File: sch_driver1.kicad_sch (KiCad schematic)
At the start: 17 parts, among them Q1 PSMN4R0-30YLDX, U1 ADA4099-2xR, U11 TS5A3159ADCK, U21 OPA333

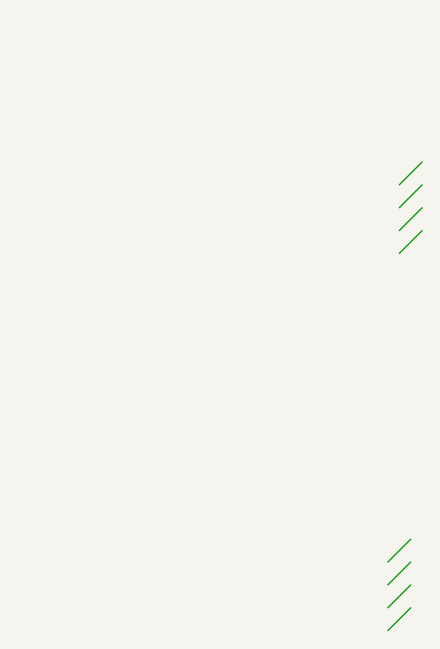
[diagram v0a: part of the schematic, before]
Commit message: Finished schematic refactor to six A-sheets. Updated PCB.
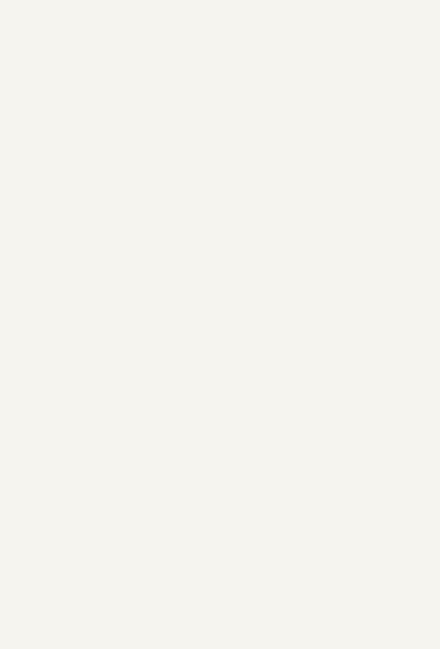
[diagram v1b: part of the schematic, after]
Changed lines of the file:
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@@
 	(title_block
 		(title "PBM Driver 4 V2")
-		(date "23-DEC-2025")
+		(date "24-DEC-2025")
 		(rev "A")
 		(comment 1 "Part Number: PCB104 Rev A")
@@
 		(color 0 0 0 0)
 	)
-	(bus_entry
-		(at 389.89 226.06)
-		(size -2.54 2.54)
-		(stroke
-			(width 0)
-			(type default)
-		)
-	)
-	(bus_entry
-		(at 389.89 223.52)
-		(size -2.54 2.54)
-		(stroke
-			(width 0)
-			(type default)
-		)
-	)
-	(bus_entry
-		(at 391.16 181.61)
-		(size -2.54 2.54)
-		(stroke
-			(width 0)
-			(type default)
-		)
-	)
-	(bus_entry
-		(at 391.16 179.07)
-		(size -2.54 2.54)
-		(stroke
-			(width 0)
-			(type default)
-		)
-	)
-	(bus_entry
-		(at 389.89 220.98)
-		(size -2.54 2.54)
-		(stroke
-			(width 0)
-			(type default)
-		)
-	)
-	(bus_entry
-		(at 391.16 184.15)
-		(size -2.54 2.54)
-		(stroke
-			(width 0)
-			(type default)
-		)
-	)
-	(bus_entry
-		(at 391.16 176.53)
-		(size -2.54 2.54)
-		(stroke
-			(width 0)
-			(type default)
-		)
-	)
-	(bus_entry
-		(at 389.89 218.44)
-		(size -2.54 2.54)
-		(stroke
-			(width 0)
-			(type default)
-		)
-	)
 	(wire

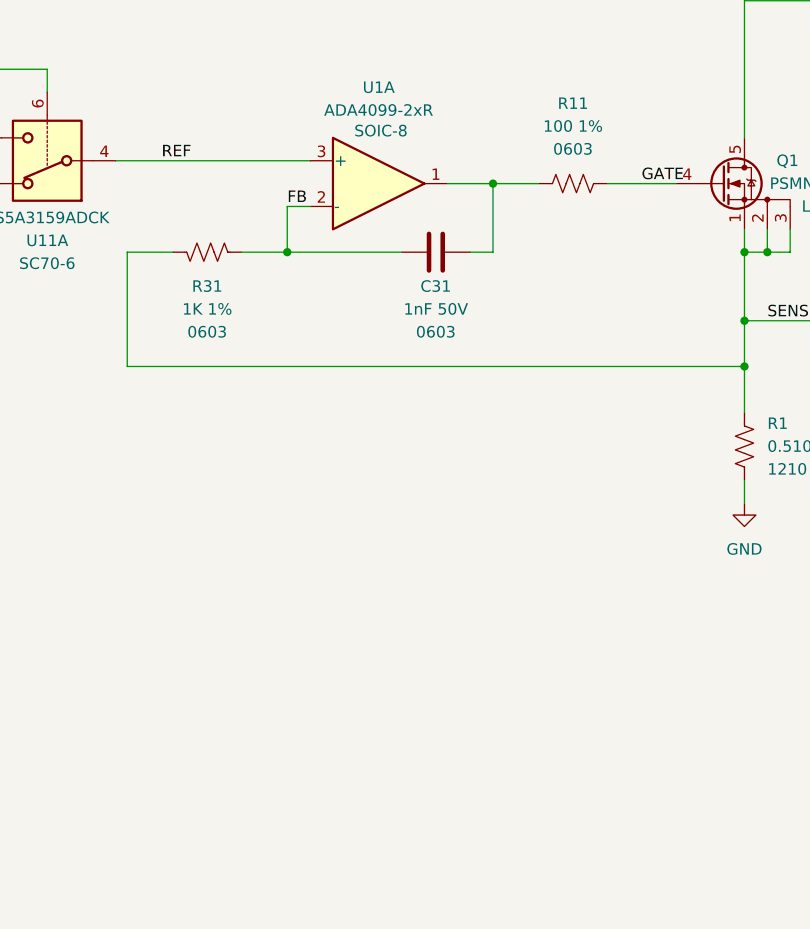
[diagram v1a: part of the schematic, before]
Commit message: Routing WIP. Prep to look at SOT-23 op amps for U1 and U2. Added convenience link to Git Bash.
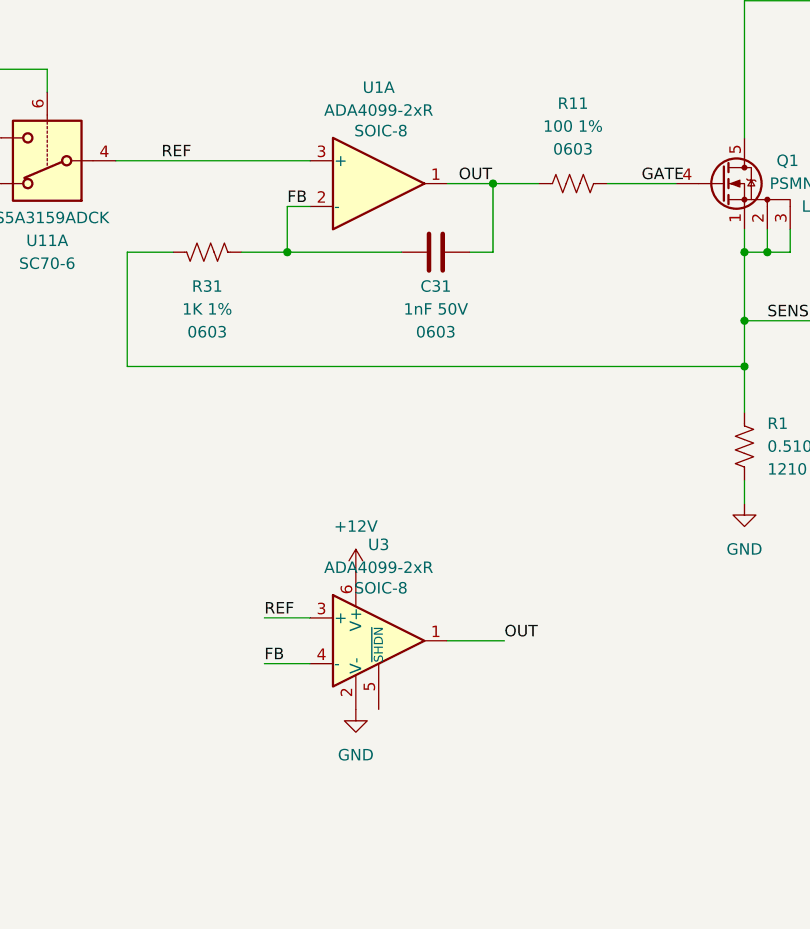
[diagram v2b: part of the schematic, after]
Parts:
- added U3: ADA4099-2xR, Package_TO_SOT_SMD:TSOT-23-6, symbol Amplifier_Operational:ADA4099-1xUJ
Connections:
- net +12V: now also U3.6 (V+)
- net FB: now also U3.4 (-)
- net GND: now also U3.2 (V-)
- net REF: now also U3.3 (+)
- net OUT: now reaches C31.2, R11.1, U1.1
- net OUT: now also U3.1

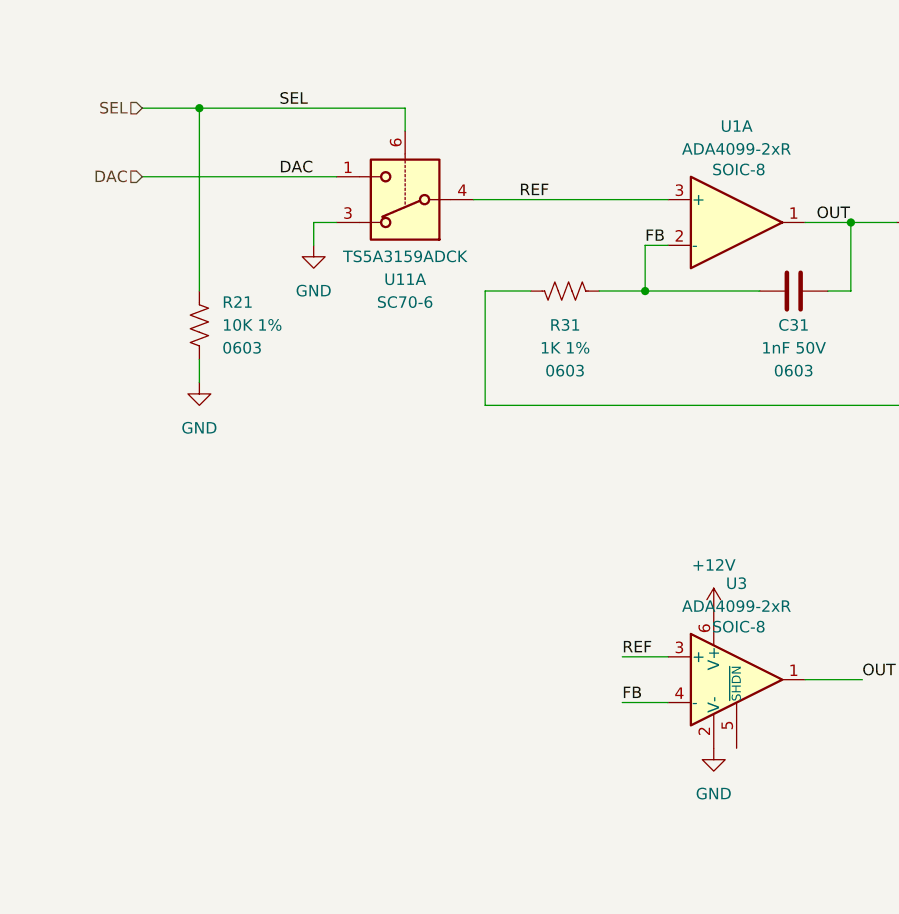
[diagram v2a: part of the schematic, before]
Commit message: Routing WIP with SOT-23 op amps
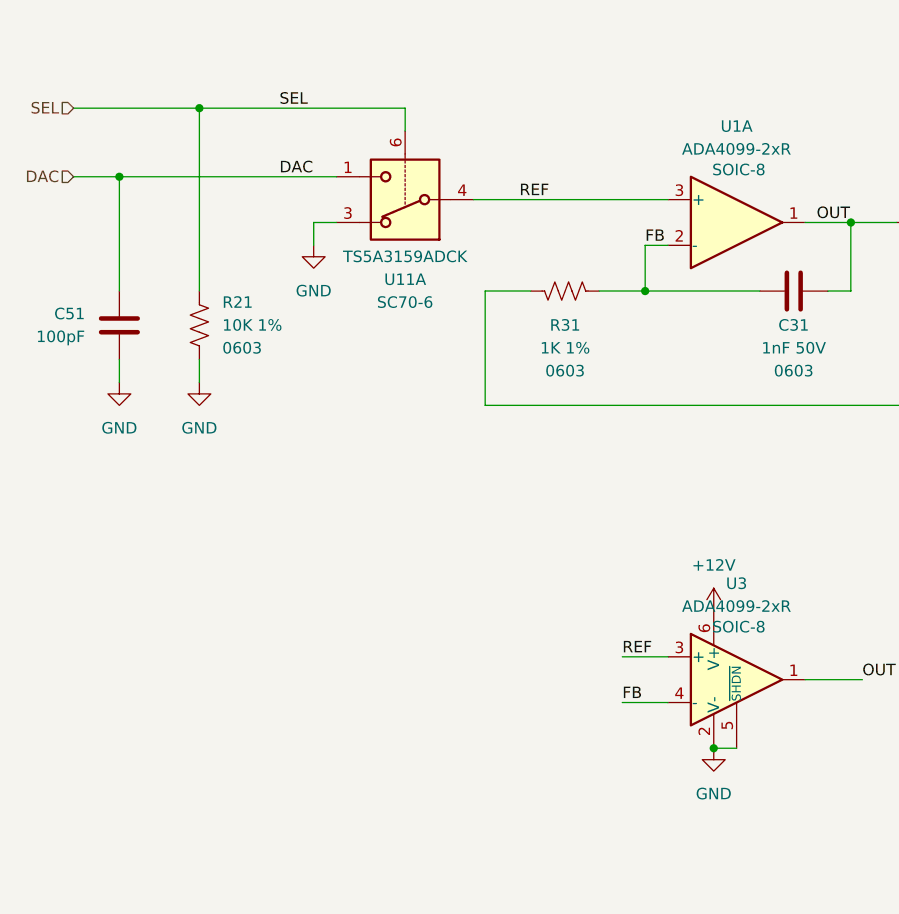
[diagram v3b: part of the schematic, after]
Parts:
- added C51: 100pF, $Local:C_0603_1608Metric, symbol $Local:C
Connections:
- net DAC: now also C51.1
- net GND: now also U3.5 (~{SHDN}), C51.2
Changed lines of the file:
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@@
+	)
+	(junction
+		(at 33.02 48.26)
+		(diameter 0)
+		(color 0 0 0 0)
 	)
 	(junction
@@
 	)
 	(junction
+		(at 99.06 111.76)
+		(diameter 0)
+		(color 0 0 0 0)
+	)
+	(junction
 		(at 95.25 147.32)
 		(diameter 0)
@@
 	(wire
 		(pts
+			(xy 99.06 111.76) (xy 101.6 111.76)
+		)
+		(stroke
+			(width 0)
+			(type default)
+		)
+	)
+	(wire
+		(pts
 			(xy 118.11 177.8) (xy 95.25 177.8)
 		)
@@
 	(wire
 		(pts
+			(xy 33.02 48.26) (xy 33.02 60.96)
+		)
+		(stroke
+			(width 0)
+			(type default)
+		)
+	)
+	(wire
+		(pts
 			(xy 203.2 88.9) (xy 205.74 88.9)
 		)
@@
 	(wire
 		(pts
-			(xy 35.56 40.64) (xy 41.91 40.64)
+			(xy 27.94 40.64) (xy 41.91 40.64)
 		)
 		(stroke
@@
 	(wire
 		(pts
-			(xy 35.56 48.26) (xy 57.15 48.26)
+			(xy 27.94 48.26) (xy 33.02 48.26)
 		)
 		(stroke
@@
 	(wire
 		(pts
+			(xy 33.02 48.26) (xy 57.15 48.26)
+		)
+		(stroke
+			(width 0)
+			(type default)
+		)
+	)
+	(wire
+		(pts
 			(xy 213.36 43.18) (xy 220.98 43.18)
 		)
@@
 		(pts
 			(xy 73.66 177.8) (xy 73.66 181.61)
+		)
+		(stroke
+			(width 0)
+			(type default)
+		)
+	)
+	(wire
+		(pts
+			(xy 33.02 68.58) (xy 33.02 71.12)
 		)
 		(stroke
@@
 	(hierarchical_label "DAC"
 		(shape input)
-		(at 35.56 48.26 180)
+		(at 27.94 48.26 180)
 		(effects
 			(font
@@
 	(hierarchical_label "SEL"
 		(shape input)
-		(at 35.56 40.64 180)
+		(at 27.94 40.64 180)
 		(effects
 			(font
@@
 	)
 	(symbol
+		(lib_id "$Local:GND")
+		(at 33.02 71.12 0)
+		(unit 1)
+		(exclude_from_sim no)
+		(in_bom yes)
+		(on_board yes)
+		(dnp no)
+		(fields_autoplaced yes)
+		(property "Reference" "#PWR021"
+			(at 33.02 77.47 0)
+			(effects
+				(font
+					(size 1.27 1.27)
+				)
+				(hide yes)
+			)
+		)
+		(property "Value" "GND"
+			(at 33.02 76.2 0)
+			(effects
+				(font
+					(size 1.27 1.27)
+				)
+			)
+		)
+		(property "Footprint" ""
+			(at 33.02 71.12 0)
+			(effects
+				(font
+					(size 1.27 1.27)
+				)
+				(hide yes)
+			)
+		)
+		(property "Datasheet" ""
+			(at 33.02 71.12 0)
+			(effects
+				(font
+					(size 1.27 1.27)
+				)
+				(hide yes)
+			)
+		)
+		(property "Description" "Power symbol creates a global label with name \"GND\" , ground"
+			(at 33.02 71.12 0)
+			(effects
+				(font
+					(size 1.27 1.27)
+				)
+				(hide yes)
+			)
+		)
+		(pin "1"
+		)
+		(instances
+			(project "pbm_driver4_v2"
+				(path "/04797749-7aaf-42f7-a5f4-0b9aeb0ad7be/69524e69-370d-45a1-972c-d2766add5424"
+					(reference "#PWR021")
+					(unit 1)
+				)
+			)
+		)
+	)
+	(symbol
 		(lib_id "$Local:C_0603_1NF_50V")
 		(at 184.15 73.66 0)
@@
 					(unit 1)
 				)
+			)
+		)
+	)
+	(symbol
+		(lib_id "$Local:C")
+		(at 33.02 64.77 0)
+		(unit 1)
+		(exclude_from_sim no)
+		(in_bom yes)
+		(on_board yes)
+		(dnp no)
+		(property "Reference" "C51"
+			(at 29.21 63.4999 0)
+			(effects
+				(font
+					(size 1.27 1.27)
+				)
+				(justify right)
+			)
+		)
+		(property "Value" "100pF"
+			(at 29.21 66.0399 0)
+			(effects
+				(font
+					(size 1.27 1.27)
+				)
+				(justify right)
+			)
+		)
+		(property "Footprint" "$Local:C_0603_1608Metric"
+			(at 33.9852 68.58 0)
+			(effects
+				(font
+					(size 1.27 1.27)
+				)
+				(hide yes)
+			)
+		)
+		(property "Datasheet" "~"
+			(at 33.02 64.77 0)
+			(effects
+				(font
+					(size 1.27 1.27)
+				)
+				(hide yes)
+			)
+		)
+		(property "Description" "Unpolarized capacitor"
+			(at 33.02 64.77 0)
+			(effects
+				(font
+					(size 1.27 1.27)
+				)
+				(hide yes)
+			)
+		)
+		(pin "2"
+		)
+		(pin "1"
+		)
+		(instances
+			(project ""
+				(path "/04797749-7aaf-42f7-a5f4-0b9aeb0ad7be/69524e69-370d-45a1-972c-d2766add5424"
+					(reference "C51")
+					(unit 1)
+				)

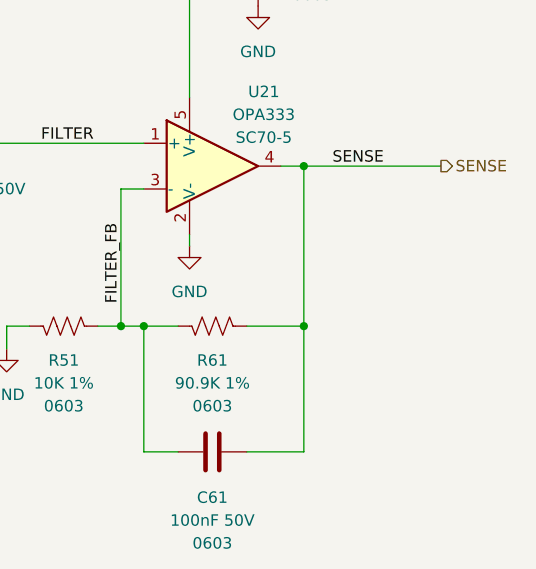
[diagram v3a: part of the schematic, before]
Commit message: Added pull-downs to output of Sense filter op amps
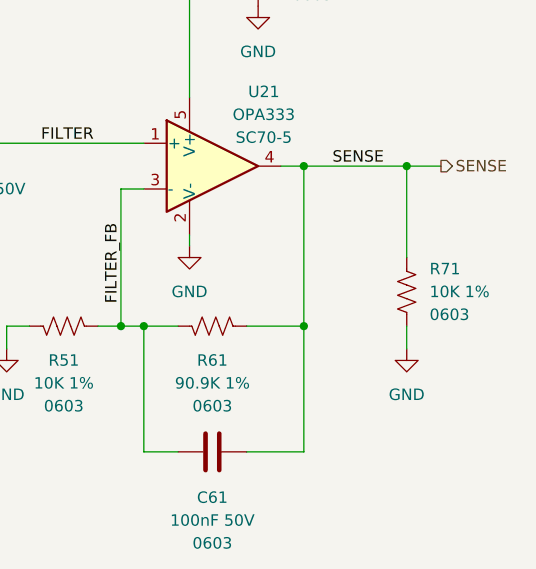
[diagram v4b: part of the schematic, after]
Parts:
- added R71: 10K 1%, $Local:R_0603_1608Metric, symbol $Local:R_0603_10K
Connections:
- net GND: now also R71.2
- net SENSE: now also R71.1
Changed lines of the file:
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@@
 	)
 	(junction
+		(at 237.49 71.12)
+		(diameter 0)
+		(color 0 0 0 0)
+	)
+	(junction
 		(at 95.25 147.32)
 		(diameter 0)
@@
 	(wire
 		(pts
+			(xy 237.49 71.12) (xy 237.49 81.28)
+		)
+		(stroke
+			(width 0)
+			(type default)
+		)
+	)
+	(wire
+		(pts
 			(xy 33.02 48.26) (xy 57.15 48.26)
 		)
@@
 	(wire
 		(pts
+			(xy 237.49 71.12) (xy 241.3 71.12)
+		)
+		(stroke
+			(width 0)
+			(type default)
+		)
+	)
+	(wire
+		(pts
 			(xy 73.66 171.45) (xy 73.66 177.8)
 		)
@@
 	(wire
 		(pts
+			(xy 237.49 88.9) (xy 237.49 91.44)
+		)
+		(stroke
+			(width 0)
+			(type default)
+		)
+	)
+	(wire
+		(pts
 			(xy 41.91 68.58) (xy 41.91 71.12)
 		)
@@
 	(wire
 		(pts
-			(xy 226.06 71.12) (xy 241.3 71.12)
+			(xy 226.06 71.12) (xy 237.49 71.12)
 		)
 		(stroke
@@
 	)
 	(symbol
+		(lib_id "$Local:R_0603_10K")
+		(at 237.49 85.09 0)
+		(unit 1)
+		(exclude_from_sim no)
+		(in_bom yes)
+		(on_board yes)
+		(dnp no)
+		(fields_autoplaced yes)
+		(property "Reference" "R71"
+			(at 240.03 82.5499 0)
+			(effects
+				(font
+					(size 1.27 1.27)
+				)
+				(justify left)
+			)
+		)
+		(property "Value" "10K 1%"
+			(at 240.03 85.0899 0)
+			(effects
+				(font
+					(size 1.27 1.27)
+				)
+				(justify left)
+			)
+		)
+		(property "Footprint" "$Local:R_0603_1608Metric"
+			(at 238.506 85.344 90)
+			(effects
+				(font
+					(size 1.27 1.27)
+				)
+				(hide yes)
+			)
+		)
+		(property "Datasheet" "~"
+			(at 237.49 85.09 0)
+			(effects
+				(font
+					(size 1.27 1.27)
+				)
+				(hide yes)
+			)
+		)
+		(property "Description" "RES SMD 10K OHM 1% 1/10W 0603"
+			(at 237.49 85.09 0)
+			(effects
+				(font
+					(size 1.27 1.27)
+				)
+				(hide yes)
+			)
+		)
+		(property "Size" "0603"
+			(at 240.03 87.6299 0)
+			(effects
+				(font
+					(size 1.27 1.27)
+				)
+				(justify left)
+			)
+		)
+		(property "PN" ""
+			(at 237.49 85.09 0)
+			(effects
+				(font
+					(size 1.27 1.27)
+				)
+				(hide yes)
+			)
+		)
+		(pin "1"
+		)
+		(pin "2"
+		)
+		(instances
+			(project ""
+				(path "/04797749-7aaf-42f7-a5f4-0b9aeb0ad7be/69524e69-370d-45a1-972c-d2766add5424"
+					(reference "R71")
+					(unit 1)
+				)
+			)
+		)
+	)
+	(symbol
 		(lib_id "$Local:C_0603_100NF_50V")
 		(at 220.98 49.53 0)
@@
 					(unit 1)
 				)
+			)
+		)
+	)
+	(symbol
+		(lib_id "$Local:GND")
+		(at 237.49 91.44 0)
+		(unit 1)
+		(exclude_from_sim no)
+		(in_bom yes)
+		(on_board yes)
+		(dnp no)
+		(fields_autoplaced yes)
+		(property "Reference" "#PWR034"
+			(at 237.49 97.79 0)
+			(effects
+				(font
+					(size 1.27 1.27)
+				)
+				(hide yes)
+			)
+		)
+		(property "Value" "GND"
+			(at 237.49 96.52 0)
+			(effects
+				(font
+					(size 1.27 1.27)
+				)
+			)
+		)
+		(property "Footprint" ""
+			(at 237.49 91.44 0)
+			(effects
+				(font
+					(size 1.27 1.27)
+				)
+				(hide yes)
+			)
+		)
+		(property "Datasheet" ""
+			(at 237.49 91.44 0)
+			(effects
+				(font
+					(size 1.27 1.27)
+				)
+				(hide yes)
+			)
+		)
+		(property "Description" "Power symbol creates a global label with name \"GND\" , ground"
+			(at 237.49 91.44 0)
+			(effects
+				(font
+					(size 1.27 1.27)
+				)
+				(hide yes)
+			)
+		)
+		(pin "1"
+		)
+		(instances
+			(project "pbm_driver4_v2"
+				(path "/04797749-7aaf-42f7-a5f4-0b9aeb0ad7be/69524e69-370d-45a1-972c-d2766add5424"
+					(reference "#PWR034")
+					(unit 1)
+				)
